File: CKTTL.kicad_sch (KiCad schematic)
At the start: 10 parts, among them Q1 BC817, U3 LM7805_TO220

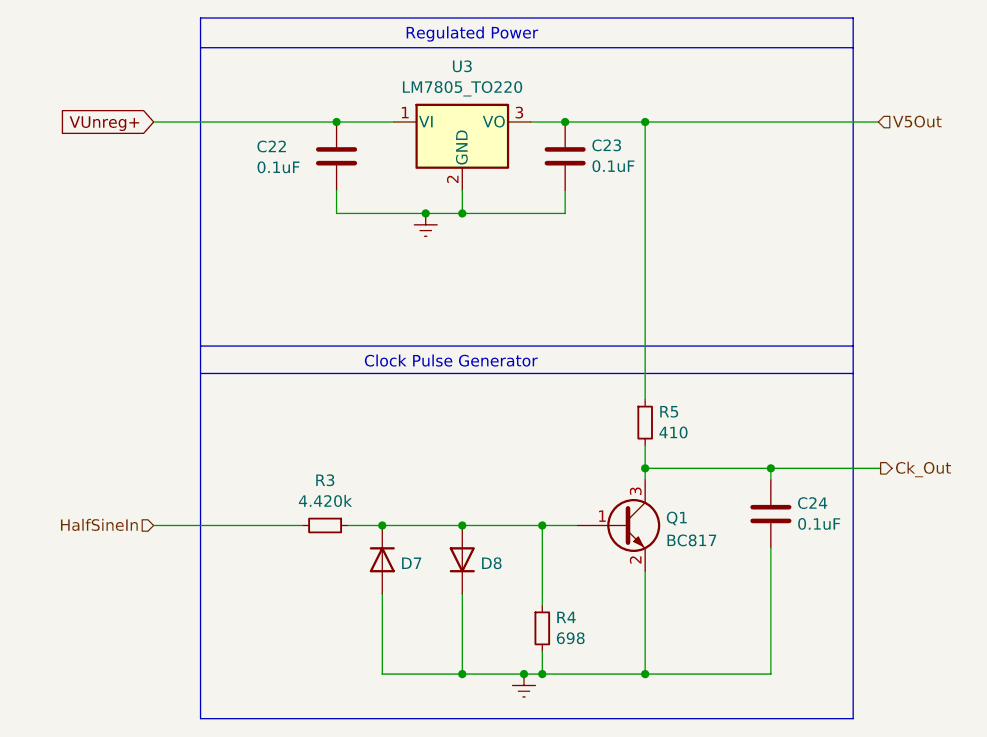
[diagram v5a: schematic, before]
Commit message: new EMC-EMI layout with improved suppression
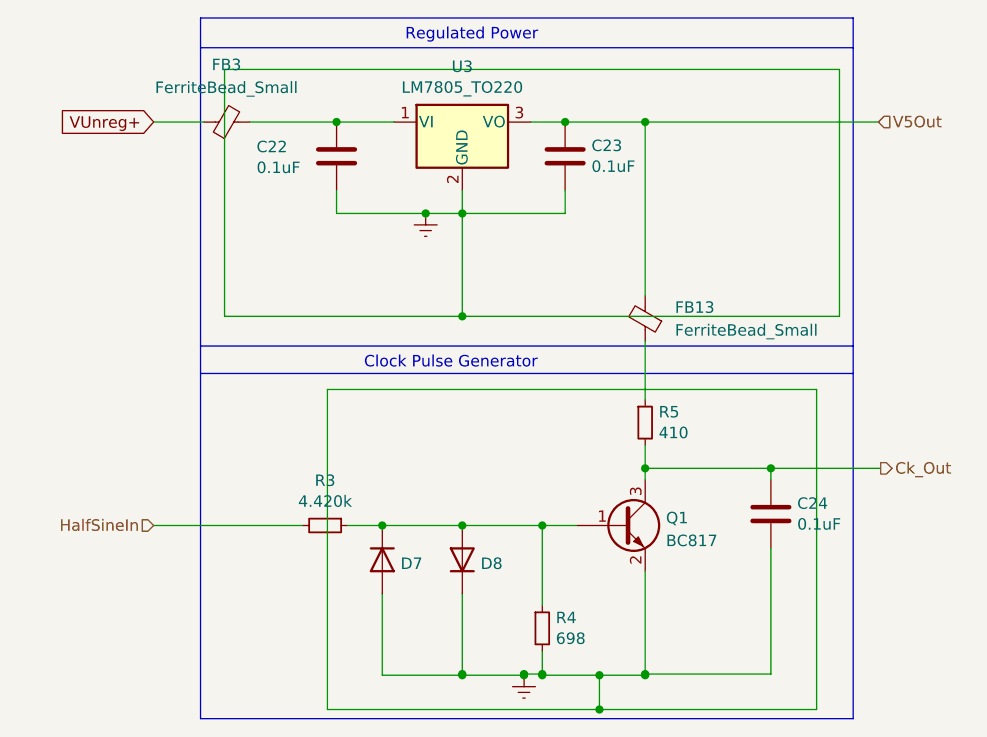
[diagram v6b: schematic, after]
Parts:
- added FB13, FB3: FerriteBead_Small, Inductor_SMD:L_0603_1608Metric, symbol Device:FerriteBead_Small
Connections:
- net V5Out: now also FB13.2; no longer R5.1
- net VUnreg+: now also FB3.1; no longer C22.1, U3.1 (VI)
- new net: C22.1, FB3.2, U3.1 (VI)
- new net: FB13.1, R5.1
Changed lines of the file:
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@@
   (junction (at 135.89 49.53) (diameter 0) (color 0 0 0 0)
   )
+  (junction (at 156.21 100.838) (diameter 0) (color 0 0 0 0)
+  )
   (junction (at 135.89 84.201) (diameter 0) (color 0 0 0 0)
   )
   (junction (at 142.748 100.711) (diameter 0) (color 0 0 0 0)
   )
+  (junction (at 144.78 100.838) (diameter 0) (color 0 0 0 0)
+  )
+  (junction (at 135.89 100.838) (diameter 0) (color 0 0 0 0)
+  )
   (junction (at 170.18 77.851) (diameter 0) (color 0 0 0 0)
   )
+  (junction (at 142.748 100.838) (diameter 0) (color 0 0 0 0)
+  )
   (junction (at 156.21 39.37) (diameter 0) (color 0 0 0 0)
   )
+  (junction (at 151.13 100.838) (diameter 0) (color 0 0 0 0)
+  )
+  (junction (at 135.89 60.96) (diameter 0) (color 0 0 0 0)
+  )
   (junction (at 144.78 84.201) (diameter 0) (color 0 0 0 0)
   )
@@
   (junction (at 156.21 100.711) (diameter 0) (color 0 0 0 0)
   )
+  (junction (at 151.13 104.648) (diameter 0) (color 0 0 0 0)
+  )
   (wire (pts (xy 135.89 46.99) (xy 135.89 49.53))
     (stroke (width 0) (type default) (color 0 0 0 0))
@@
     (stroke (width 0) (type default) (color 0 0 0 0))
   )
-  (wire (pts (xy 127 100.711) (xy 135.89 100.711))
+  (wire (pts (xy 127 100.838) (xy 135.89 100.838))
     (stroke (width 0) (type default) (color 0 0 0 0))
   )
@@
     (stroke (width 0) (type default) (color 0 0 0 0))
   )
-  (wire (pts (xy 144.78 100.711) (xy 156.21 100.711))
+  (wire (pts (xy 144.78 100.838) (xy 151.13 100.838))
     (stroke (width 0) (type default) (color 0 0 0 0))
   )
@@
     (stroke (width 0) (type default) (color 0 0 0 0))
   )
+  (wire (pts (xy 135.89 49.53) (xy 135.89 60.96))
+    (stroke (width 0) (type default) (color 0 0 0 0))
+  )
   (wire (pts (xy 156.21 89.281) (xy 156.21 100.711))
     (stroke (width 0) (type default) (color 0 0 0 0))
   )
+  (wire (pts (xy 156.21 100.838) (xy 156.21 100.711))
+    (stroke (width 0) (type default) (color 0 0 0 0))
+  )
   (wire (pts (xy 156.21 75.311) (xy 156.21 77.851))
     (stroke (width 0) (type default) (color 0 0 0 0))
   )
+  (wire (pts (xy 109.474 33.528) (xy 109.474 60.96))
+    (stroke (width 0) (type default) (color 0 0 0 0))
+  )
   (wire (pts (xy 156.21 100.711) (xy 170.18 100.711))
     (stroke (width 0) (type default) (color 0 0 0 0))
@@
     (stroke (width 0) (type default) (color 0 0 0 0))
   )
+  (wire (pts (xy 120.904 104.648) (xy 151.13 104.648))
+    (stroke (width 0) (type default) (color 0 0 0 0))
+  )
   (polyline (pts (xy 106.807 27.813) (xy 179.324 27.813))
     (stroke (width 0) (type default) (color 0 0 0 0))
   )
-  (wire (pts (xy 135.89 100.711) (xy 142.748 100.711))
+  (wire (pts (xy 135.89 100.838) (xy 142.748 100.838))
     (stroke (width 0) (type default) (color 0 0 0 0))
   )
@@
     (stroke (width 0) (type default) (color 0 0 0 0))
   )
+  (wire (pts (xy 135.89 100.838) (xy 135.89 100.711))
+    (stroke (width 0) (type default) (color 0 0 0 0))
+  )
   (wire (pts (xy 144.78 84.201) (xy 148.59 84.201))
     (stroke (width 0) (type default) (color 0 0 0 0))
@@
     (stroke (width 0) (type default) (color 0 0 0 0))
   )
+  (wire (pts (xy 120.904 69.088) (xy 120.904 104.648))
+    (stroke (width 0) (type default) (color 0 0 0 0))
+  )
   (wire (pts (xy 170.18 86.741) (xy 170.18 100.711))
     (stroke (width 0) (type default) (color 0 0 0 0))
   )
-  (wire (pts (xy 101.6 39.37) (xy 121.92 39.37))
+  (wire (pts (xy 101.6 39.37) (xy 107.188 39.37))
     (stroke (width 0) (type default) (color 0 0 0 0))
   )
@@
     (stroke (width 0) (type default) (color 0 0 0 0))
   )
-  (wire (pts (xy 156.21 39.37) (xy 156.21 70.231))
+  (wire (pts (xy 156.21 39.37) (xy 156.21 58.674))
+    (stroke (width 0) (type default) (color 0 0 0 0))
+  )
+  (wire (pts (xy 135.89 60.96) (xy 177.8 60.96))
     (stroke (width 0) (type default) (color 0 0 0 0))
   )
@@
     (stroke (width 0) (type default) (color 0 0 0 0))
   )
+  (wire (pts (xy 151.13 104.648) (xy 175.26 104.648))
+    (stroke (width 0) (type default) (color 0 0 0 0))
+  )
+  (wire (pts (xy 156.21 63.754) (xy 156.21 70.231))
+    (stroke (width 0) (type default) (color 0 0 0 0))
+  )
   (polyline (pts (xy 106.807 105.664) (xy 179.324 105.664))
     (stroke (width 0) (type default) (color 0 0 0 0))
@@
     (stroke (width 0) (type default) (color 0 0 0 0))
   )
+  (wire (pts (xy 120.904 69.088) (xy 175.26 69.088))
+    (stroke (width 0) (type default) (color 0 0 0 0))
+  )
+  (wire (pts (xy 112.268 39.37) (xy 121.92 39.37))
+    (stroke (width 0) (type default) (color 0 0 0 0))
+  )
+  (wire (pts (xy 151.13 100.838) (xy 156.21 100.838))
+    (stroke (width 0) (type default) (color 0 0 0 0))
+  )
+  (wire (pts (xy 109.474 60.96) (xy 135.89 60.96))
+    (stroke (width 0) (type default) (color 0 0 0 0))
+  )
+  (wire (pts (xy 177.8 33.528) (xy 177.8 60.96))
+    (stroke (width 0) (type default) (color 0 0 0 0))
+  )
+  (wire (pts (xy 175.26 69.088) (xy 175.26 104.648))
+    (stroke (width 0) (type default) (color 0 0 0 0))
+  )
   (wire (pts (xy 170.18 77.851) (xy 182.372 77.851))
     (stroke (width 0) (type default) (color 0 0 0 0))
@@
     (stroke (width 0) (type default) (color 0 0 0 0))
   )
+  (wire (pts (xy 142.748 100.838) (xy 142.748 100.711))
+    (stroke (width 0) (type default) (color 0 0 0 0))
+  )
   (wire (pts (xy 156.21 77.851) (xy 156.21 79.121))
     (stroke (width 0) (type default) (color 0 0 0 0))
@@
     (stroke (width 0) (type default) (color 0 0 0 0))
   )
-  (wire (pts (xy 127 91.821) (xy 127 100.711))
+  (wire (pts (xy 127 91.821) (xy 127 100.838))
+    (stroke (width 0) (type default) (color 0 0 0 0))
+  )
+  (wire (pts (xy 144.78 100.838) (xy 144.78 100.711))
+    (stroke (width 0) (type default) (color 0 0 0 0))
+  )
+  (wire (pts (xy 109.474 33.528) (xy 177.8 33.528))
+    (stroke (width 0) (type default) (color 0 0 0 0))
+  )
+  (wire (pts (xy 151.13 100.838) (xy 151.13 104.648))
     (stroke (width 0) (type default) (color 0 0 0 0))
   )
@@
     (effects (font (size 1.27 1.27)) (justify right))
   )
+  (symbol (lib_id "Device:FerriteBead_Small") (at 109.728 39.37 90) (unit 1)
+    (in_bom yes) (on_board yes) (fields_autoplaced)
+    (property "Reference" "FB3" (id 0) (at 109.6899 33.02 90))
+    (property "Value" "FerriteBead_Small" (id 1) (at 109.6899 35.56 90))
+    (property "Footprint" "Inductor_SMD:L_0603_1608Metric" (id 2) (at 109.728 41.148 90)
+      (effects (font (size 1.27 1.27)) hide)
+    )
+    (property "Datasheet" "~" (id 3) (at 109.728 39.37 0)
+      (effects (font (size 1.27 1.27)) hide)
+    )
+    (pin "1")
+    (pin "2")
+  )
+  (symbol (lib_id "Device:FerriteBead_Small") (at 156.21 61.214 180) (unit 1)
+    (in_bom yes) (on_board yes) (fields_autoplaced)
+    (property "Reference" "FB13" (id 0) (at 159.512 59.982 0)
+      (effects (font (size 1.27 1.27)) (justify right))
+    )
+    (property "Value" "FerriteBead_Small" (id 1) (at 159.512 62.522 0)
+      (effects (font (size 1.27 1.27)) (justify right))
+    )
+    (property "Footprint" "Inductor_SMD:L_0603_1608Metric" (id 2) (at 157.988 61.214 90)
+      (effects (font (size 1.27 1.27)) hide)
+    )
+    (property "Datasheet" "~" (id 3) (at 156.21 61.214 0)
+      (effects (font (size 1.27 1.27)) hide)
+    )
+    (pin "1")
+    (pin "2")
+  )
   (symbol (lib_id "Device:C") (at 170.18 82.931 0) (unit 1)
     (in_bom yes) (on_board yes)
@@
     (pin "2")
   )
-  (symbol (lib_id "power:GNDREF") (at 142.748 100.711 0) (unit 1)
-    (in_bom yes) (on_board yes) (fields_autoplaced)
-    (property "Reference" "#PWR026" (id 0) (at 142.748 107.061 0)
-      (effects (font (size 1.27 1.27)) hide)
-    )
-    (property "Value" "GNDREF" (id 1) (at 142.748 105.1544 0)
-      (effects (font (size 1.27 1.27)) hide)
-    )
-    (property "Footprint" "" (id 2) (at 142.748 100.711 0)
-      (effects (font (size 1.27 1.27)) hide)
-    )
-    (property "Datasheet" "" (id 3) (at 142.748 100.711 0)
-      (effects (font (size 1.27 1.27)) hide)
-    )
+  (symbol (lib_id "power:GNDREF") (at 142.748 100.838 0) (unit 1)
+    (in_bom yes) (on_board yes) (fields_autoplaced)
+    (property "Reference" "#PWR026" (id 0) (at 142.748 107.188 0)
+      (effects (font (size 1.27 1.27)) hide)
+    )
+    (property "Value" "GNDREF" (id 1) (at 142.748 105.2814 0)
+      (effects (font (size 1.27 1.27)) hide)
+    )
+    (property "Footprint" "" (id 2) (at 142.748 100.838 0)
+      (effects (font (size 1.27 1.27)) hide)
+    )
+    (property "Datasheet" "" (id 3) (at 142.748 100.838 0)
+      (effects (font (size 1.27 1.27)) hide)
+    )

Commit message: working on MUX and pre-amp layout
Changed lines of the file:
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@@
     (pin "2")
   )
+  (symbol (lib_id "power:PWR_FLAG") (at 121.92 39.37 0) (unit 1)
+    (in_bom yes) (on_board yes) (fields_autoplaced)
+    (property "Reference" "#FLG0112" (id 0) (at 121.92 37.465 0)
+      (effects (font (size 1.27 1.27)) hide)
+    )
+    (property "Value" "PWR_FLAG" (id 1) (at 121.92 34.29 0))
+    (property "Footprint" "" (id 2) (at 121.92 39.37 0)
+      (effects (font (size 1.27 1.27)) hide)
+    )
+    (property "Datasheet" "~" (id 3) (at 121.92 39.37 0)
+      (effects (font (size 1.27 1.27)) hide)
+    )
+    (pin "1")
+  )
 )
